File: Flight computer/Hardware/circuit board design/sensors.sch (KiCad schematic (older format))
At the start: 5 parts, among them U10 BMI088, U8 MS5607-02BA

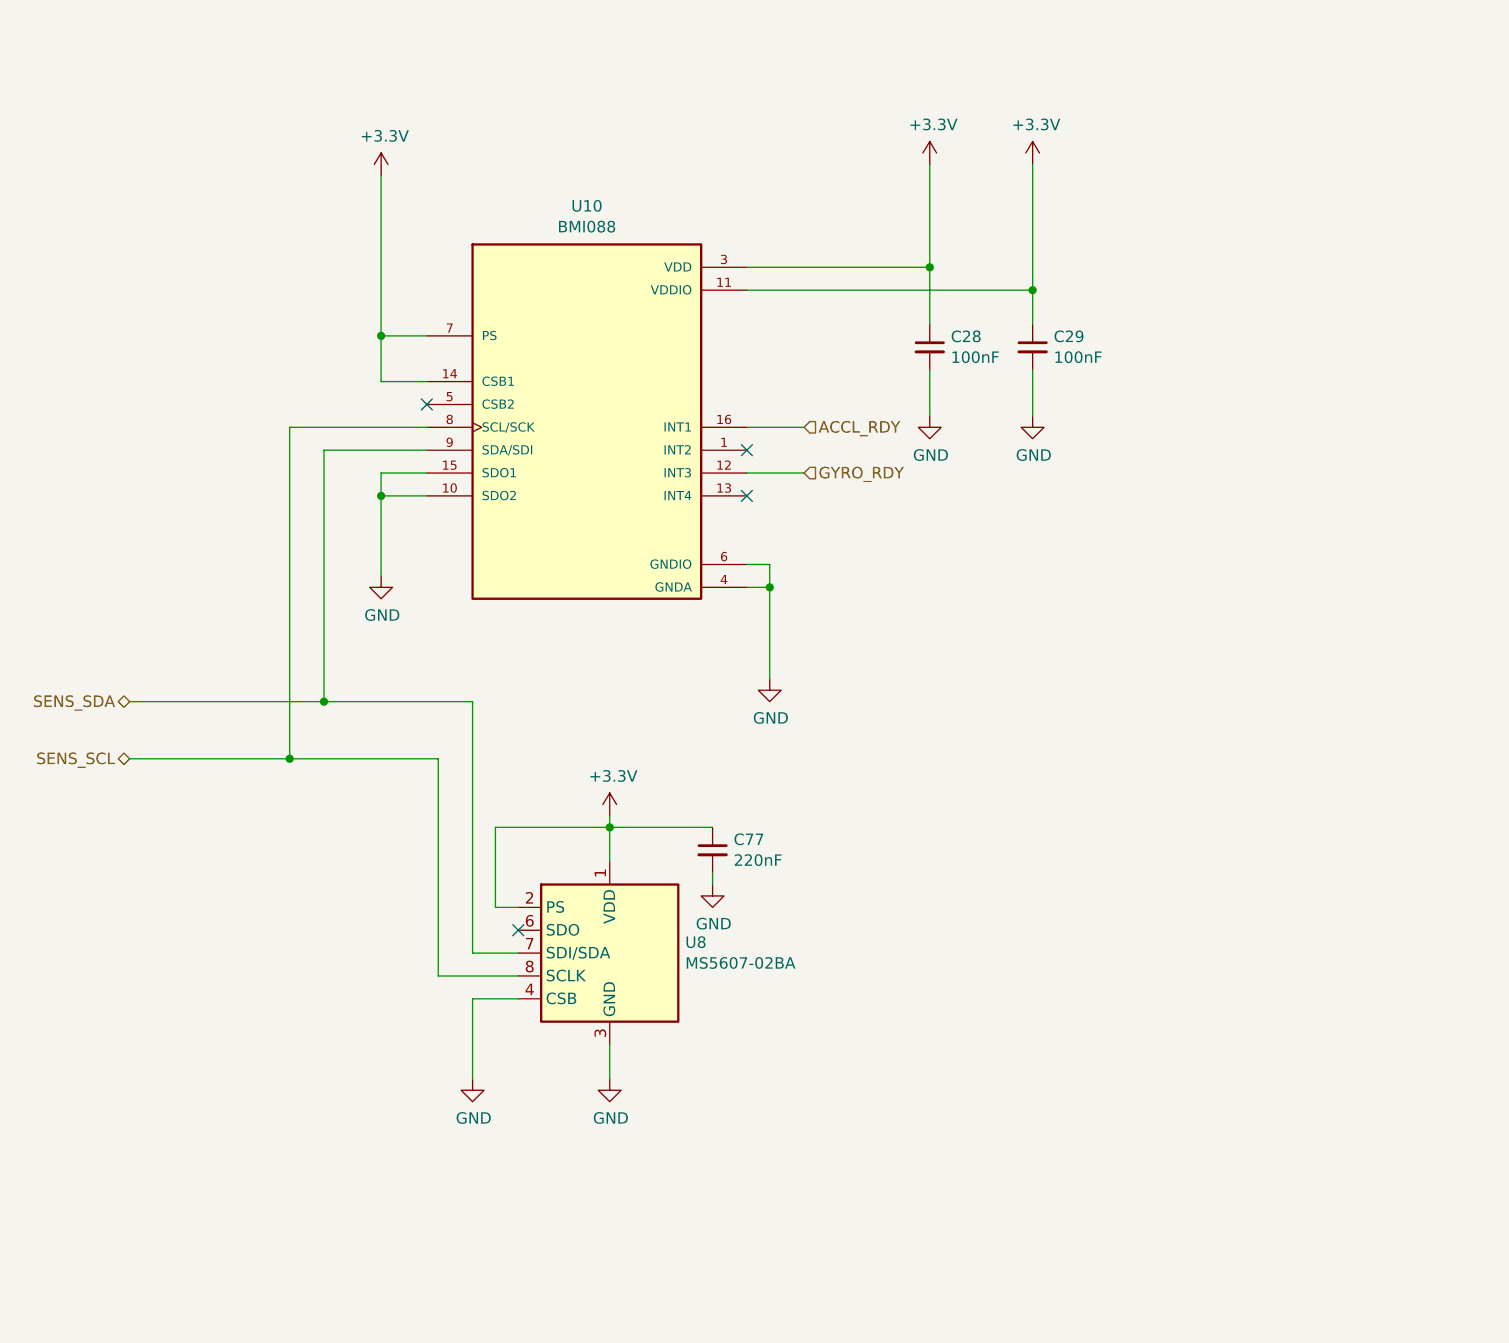
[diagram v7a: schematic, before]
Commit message: more upgrades
- removed the comparators
- added the cost and link to buy components
- added in a symbol for USB
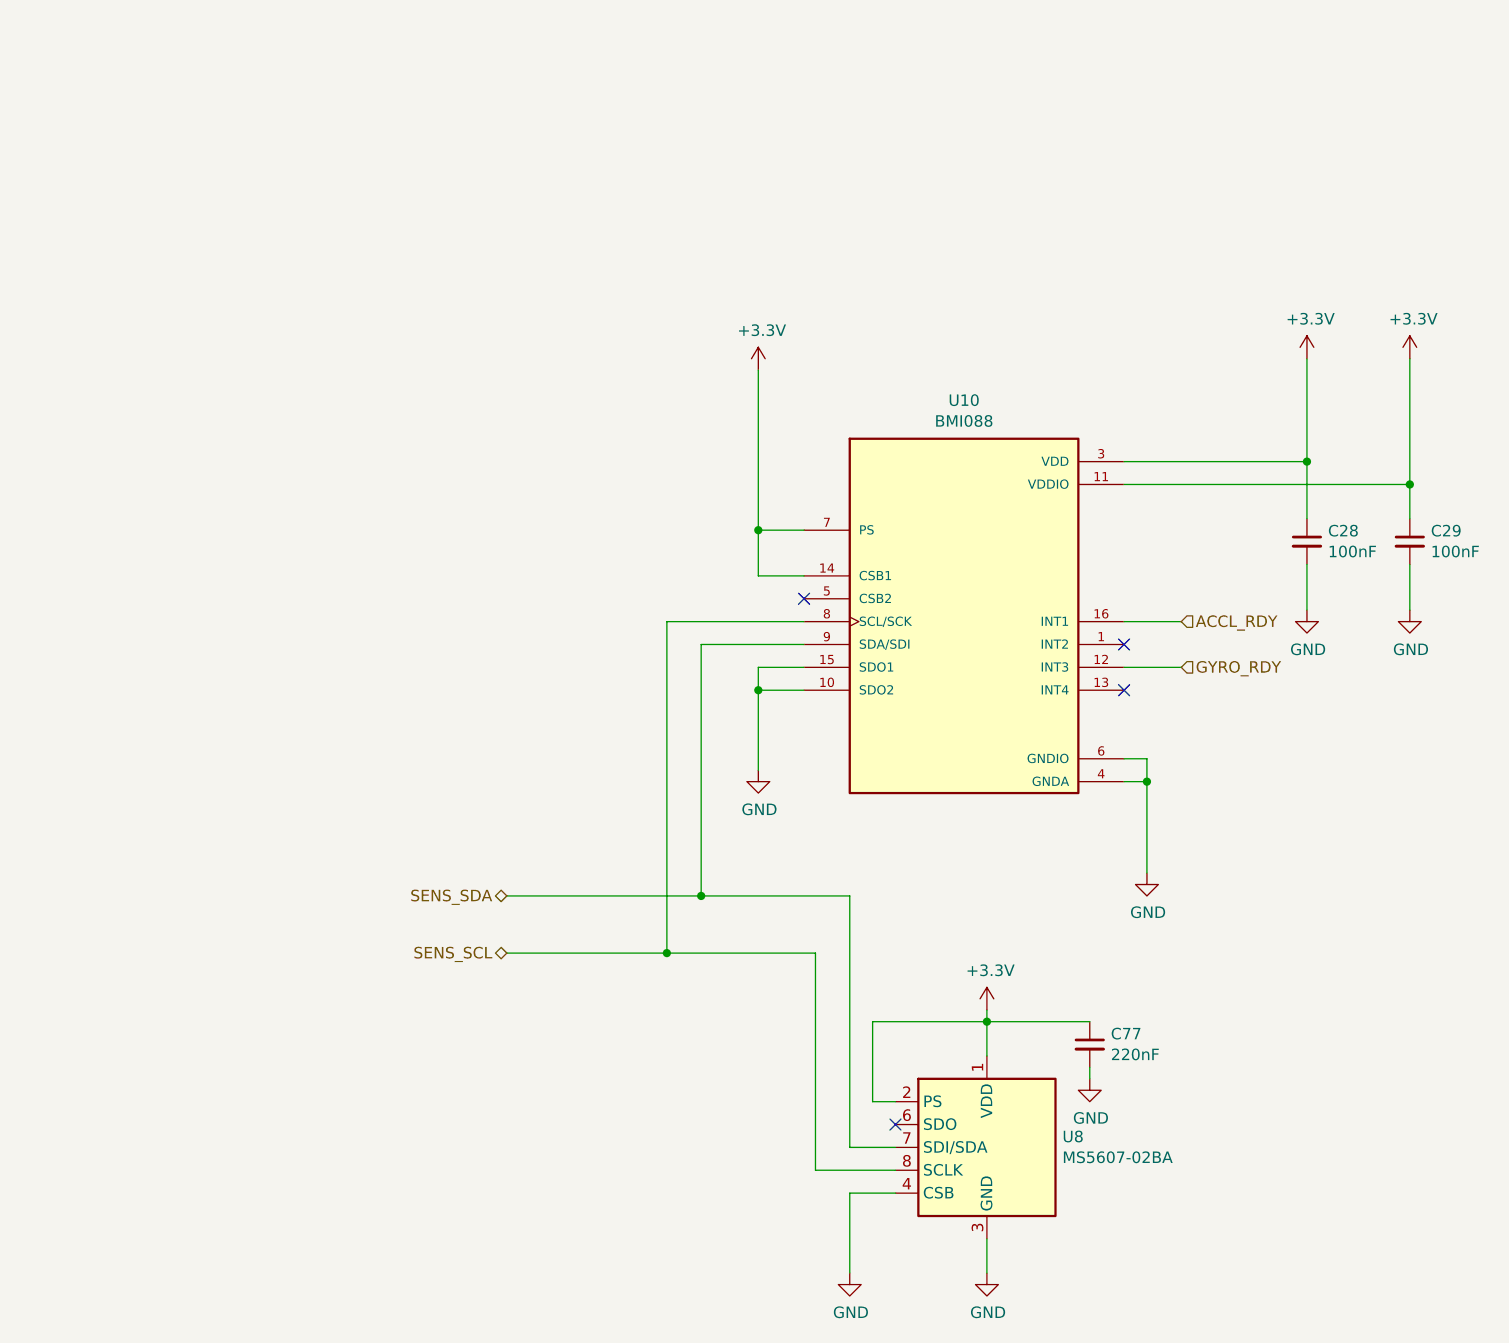
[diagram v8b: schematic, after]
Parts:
- U10: footprint flight-computer:PQFN50P450X300X100-16N -> BMI088:PQFN50P450X300X100-16N; Cost (none) -> 5.21; Field4 None -> (none); Field5 High-performance 6-axis inertial sensor _accelerometer + gy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 -> (none); Field6 BMI088 -> (none); Field7 Unavailable -> (none); Field8 VFLGA-16 Bosch Sensortec -> (none); Purchase link (none) -> https://www.mouser.co.uk/ProductDetail/Bosch-Sensortec/BMI0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
- U8: Purchase link (none) -> https://www.mouser.co.uk/ProductDetail/Measurement-Specialt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
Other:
- moved on the sheet: C28, C29, C77, U10, U8
